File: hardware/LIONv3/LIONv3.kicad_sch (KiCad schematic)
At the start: 35 parts, among them SW1 RESET, SW2 BOOT, U1 TCAN3414DR, U14 HC-1_25-2PWT, U15 HC-1_25-2PWT, U19 HC-1_25-2PWT, U2 TYPE-C_16PIN_2MD(073), U3 ESP32-C6-MINI-1-N4, U4 TMP112AIDRLR, U9 HC-1_25-2PWT

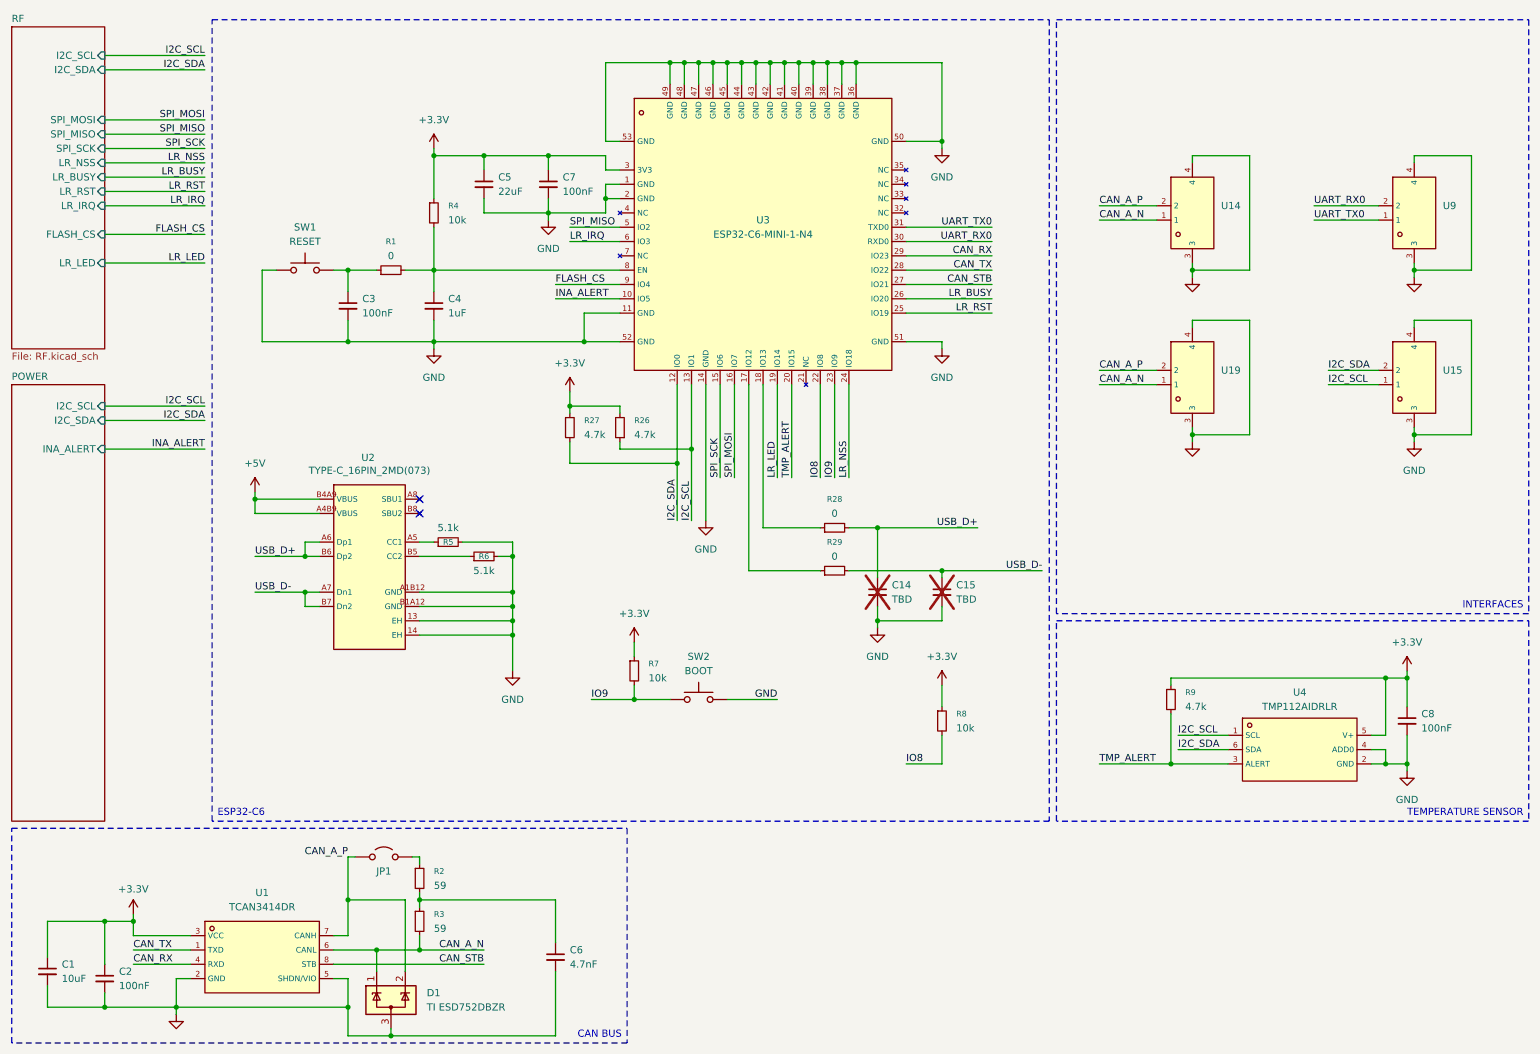
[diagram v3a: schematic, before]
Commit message: Add TVS diode protection (ESD9B3.3ST5G)
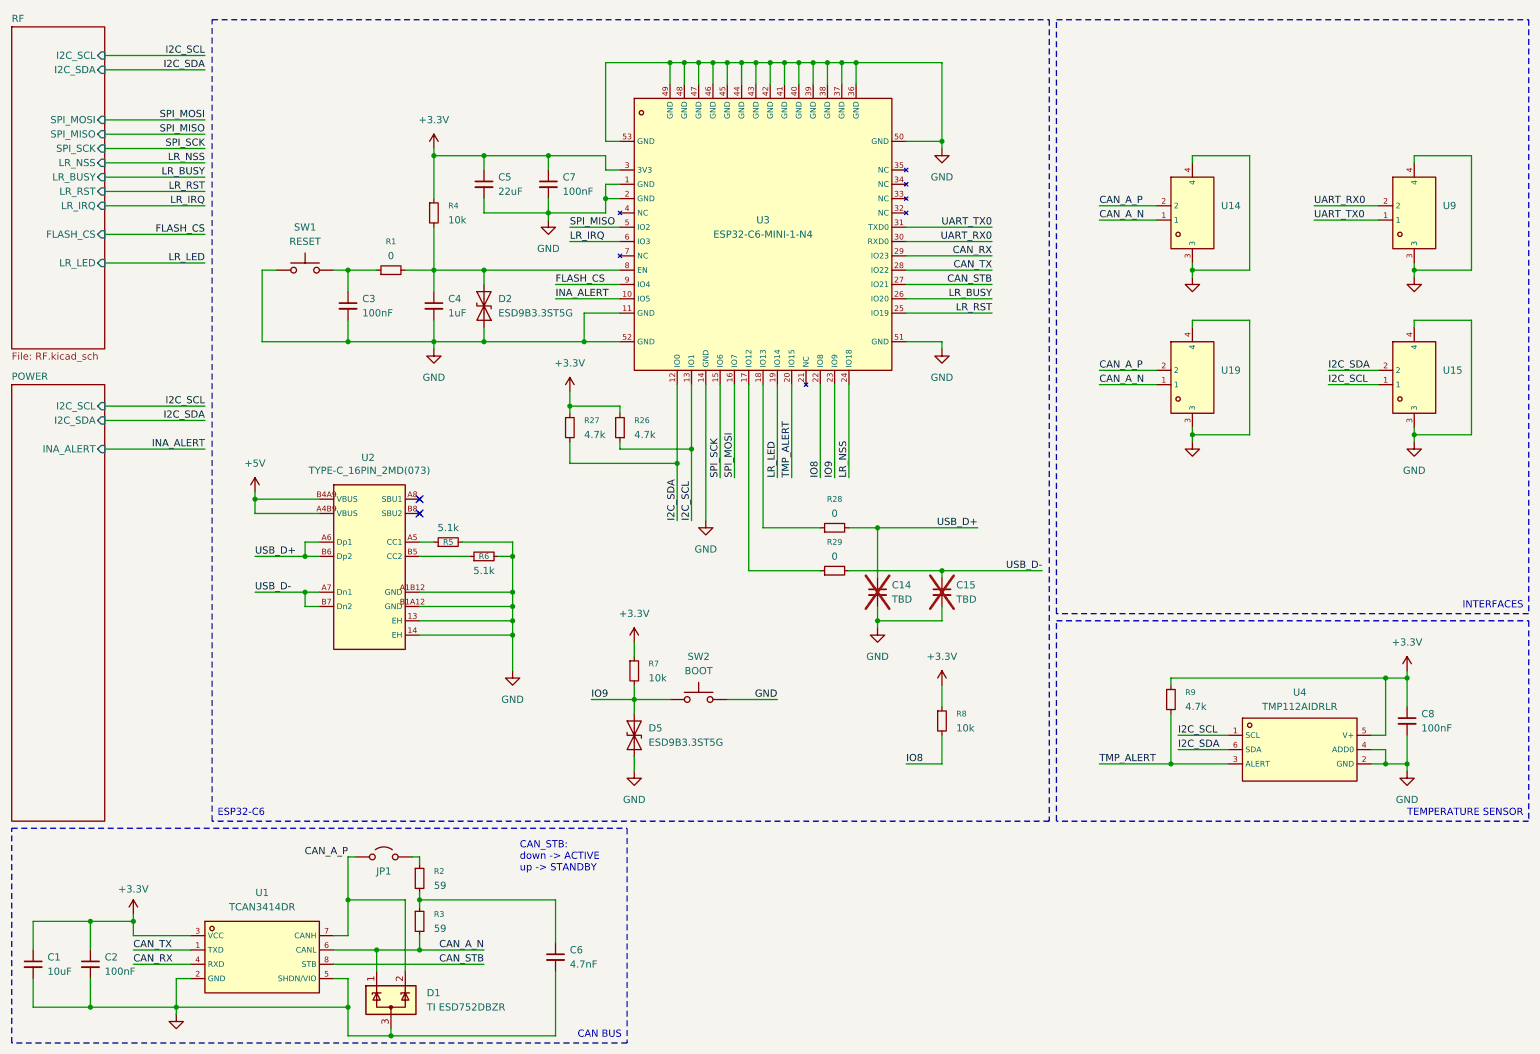
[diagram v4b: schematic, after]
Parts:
- added D2, D5: ESD9B3.3ST5G, Diode_SMD:D_SOD-923, symbol Diode:ESD9B3.3ST5G
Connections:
- net GND: now also D2.1 (A1), D5.1 (A1)
- net IO9: now also D5.2 (A2)
- net at C4.1, R1.2, R4.2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: now also D2.2 (A2)
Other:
- note added: "CAN_STB: down -> ACTIVE up -> STANDBY"
- moved on the sheet: C1, C2

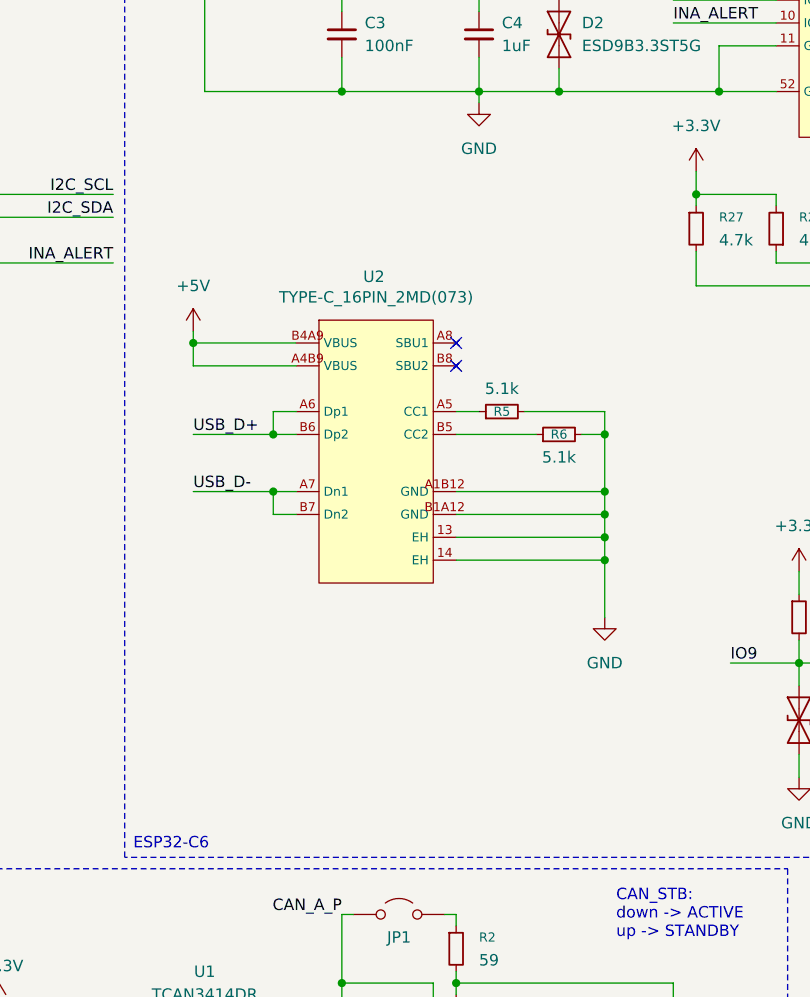
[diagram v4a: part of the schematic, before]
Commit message: feat(hardware): Add TVS diode protection on USB lines (USBLC6-2SC6)
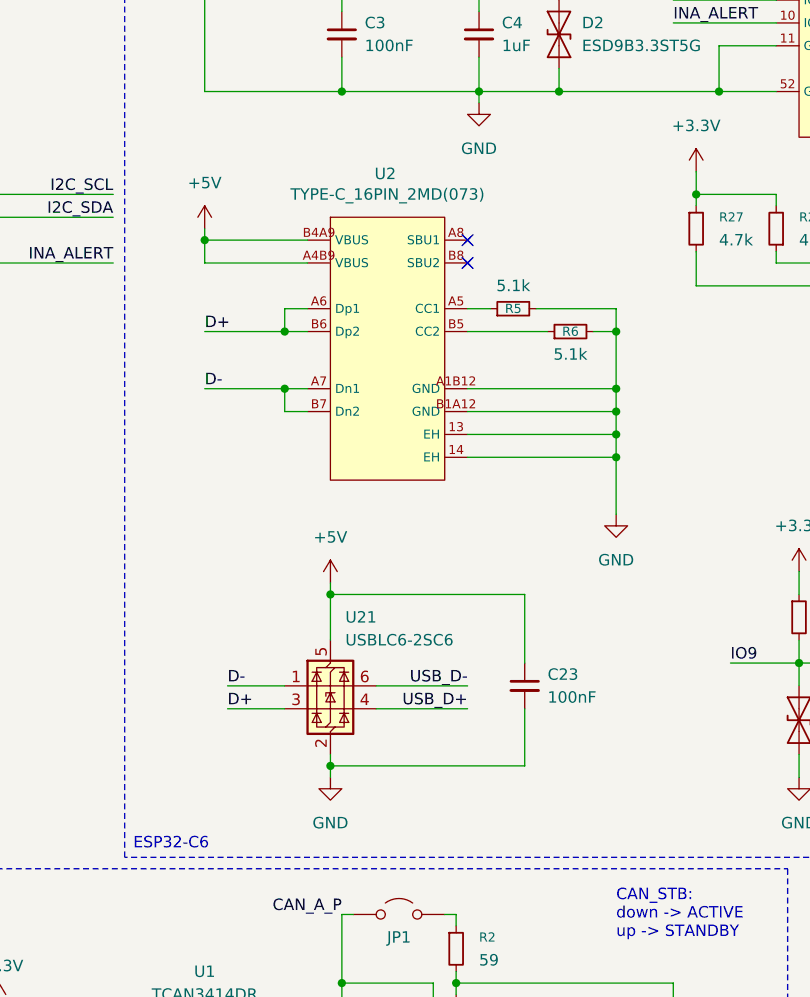
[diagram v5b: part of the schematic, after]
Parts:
- added C23: 100nF, symbol Device:C_Small
- added U21: USBLC6-2SC6, Package_TO_SOT_SMD:SOT-23-6, symbol Power_Protection:USBLC6-2SC6
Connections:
- net +5V: now also C23.1, U21.5 (VBUS)
- net GND: now also C23.2, U21.2 (GND)
- net USB_D+: now also U21.4 (I/O2); no longer U2.A6 (Dp1), U2.B6 (Dp2)
- net USB_D-: now also U21.6 (I/O1); no longer U2.A7 (Dn1), U2.B7 (Dn2)
- new net D+: U2.A6 (Dp1), U2.B6 (Dp2), U21.3 (I/O2)
- new net D-: U2.A7 (Dn1), U2.B7 (Dn2), U21.1 (I/O1)
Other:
- moved on the sheet: R5, R6, U2

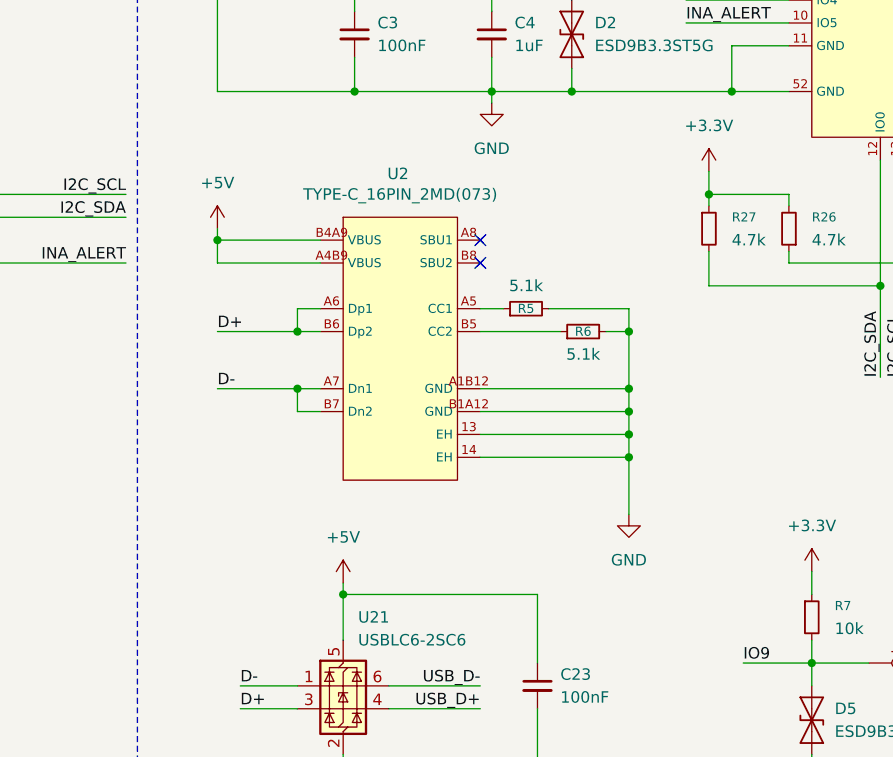
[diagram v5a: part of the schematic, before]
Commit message: feat(hardware): Add Ferrite Bead to VBUS line
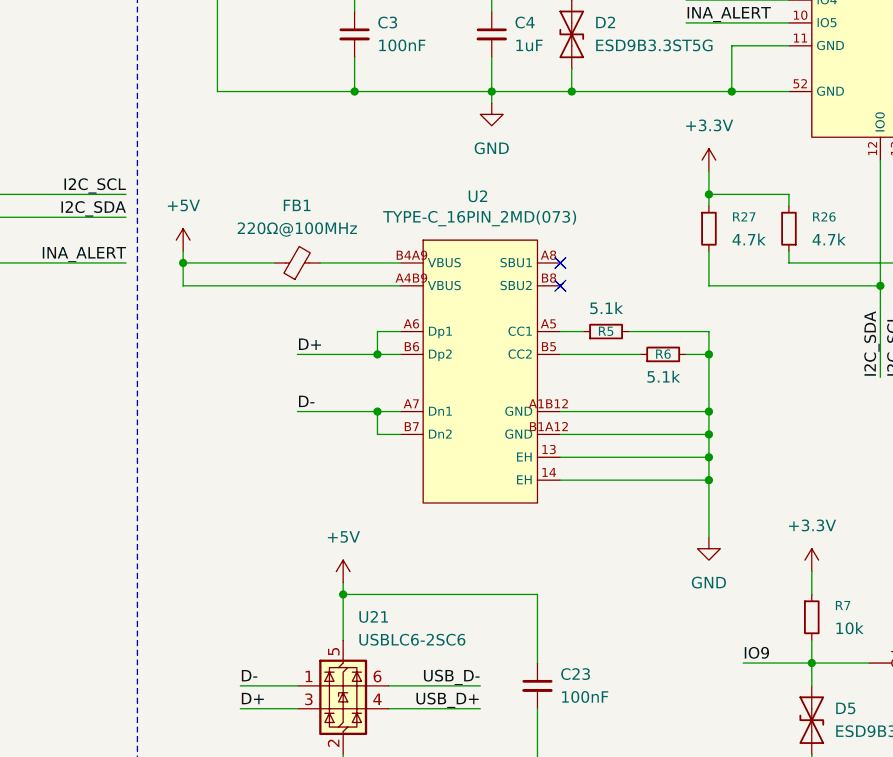
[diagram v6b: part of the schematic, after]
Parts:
- added FB1: 220Ω@100MHz, Capacitor_SMD:C_0805_2012Metric, symbol Device:FerriteBead_Small
- C23: footprint (none) -> Capacitor_SMD:C_0402_1005Metric
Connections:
- net +5V: now also FB1.1; no longer U2.B4A9 (VBUS)
- new net: FB1.2, U2.B4A9 (VBUS)
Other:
- moved on the sheet: R5, R6, U2

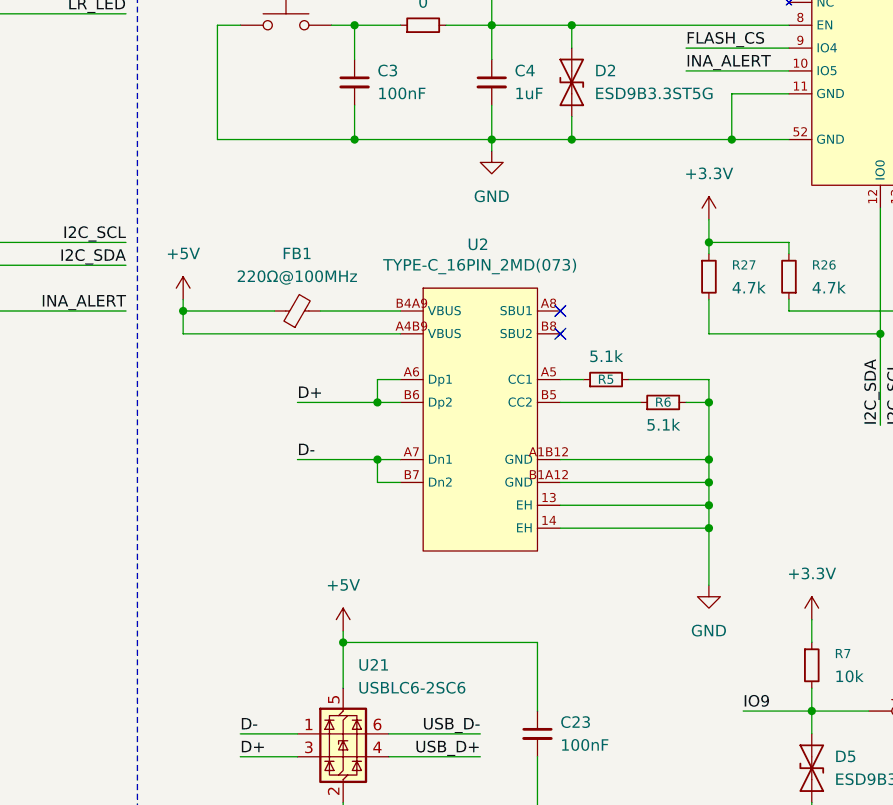
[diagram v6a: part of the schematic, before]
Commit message: feat(hardware): Add ORing (USB VBUS back-feed)
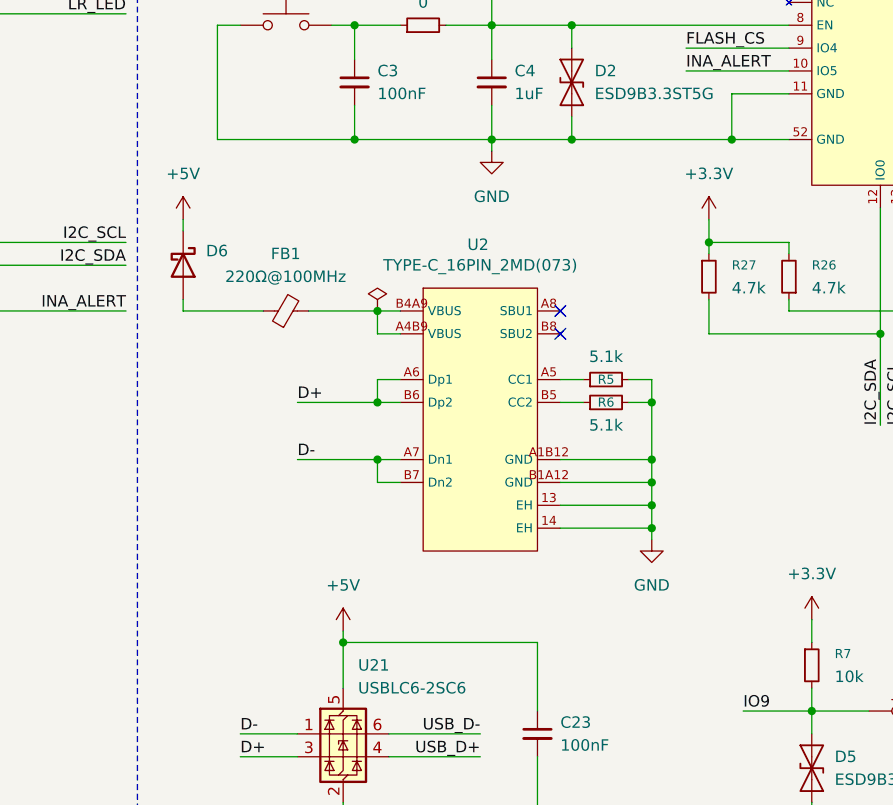
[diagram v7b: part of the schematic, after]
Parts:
- added D6: D_Schottky, LIONv3-Footprints:X2-DFN1006-2_L1.0-W0.6-P0.65-RD, symbol Device:D_Schottky
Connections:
- net +5V: now also D6.1 (K); no longer FB1.1, U2.A4B9 (VBUS)
- net at FB1.2, U2.B4A9 (VBUS): now also U2.A4B9 (VBUS)
- new net: D6.2 (A), FB1.1
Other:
- moved on the sheet: FB1, R6

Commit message: feat(hardware): removes R1 and C3 from reset switch
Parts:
- removed C3: 100nF, Capacitor_SMD:C_0402_1005Metric, symbol Device:C_Small
- removed R1: 0, Resistor_SMD:R_0402_1005Metric, symbol Device:R_Small
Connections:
- net at C4.1, D2.2 (A2), R4.2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: now also SW1.2
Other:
- note added: "High frequency filtering"
- note added: "LATCH CONNECTORS mates in one orientation only"
- moved on the sheet: D2, SW1
